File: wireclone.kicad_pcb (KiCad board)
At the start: 2 copper layers, 98.4 x 48.3 mm, 47 parts, among them P1 CONN_01X03, P2 CONN_01X02, P3 CONN_01X03, P4 CONN_01X02, U1 LME49720, U2 LME49720, U3 LME49600, U4 LME49600, U5 LM7812CT, U6 LM7912CT

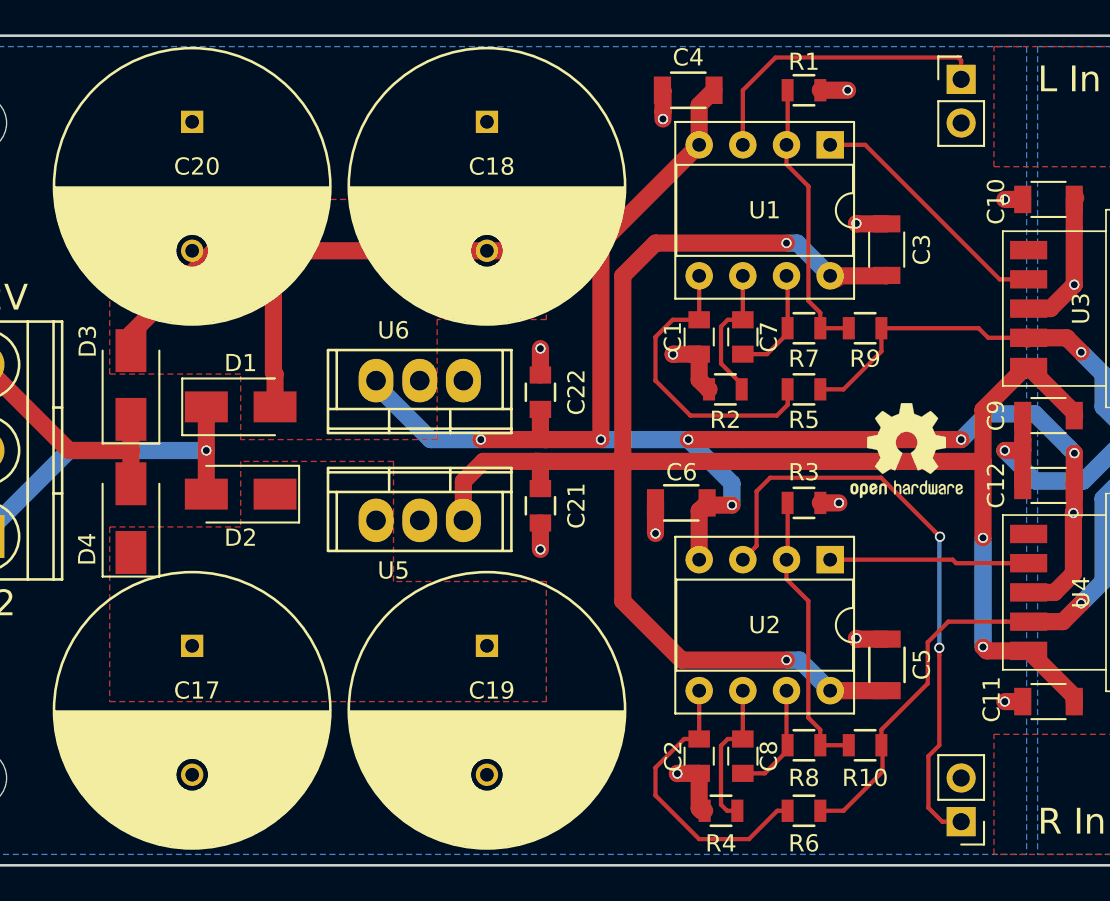
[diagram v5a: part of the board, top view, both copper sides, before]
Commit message: added fiducials
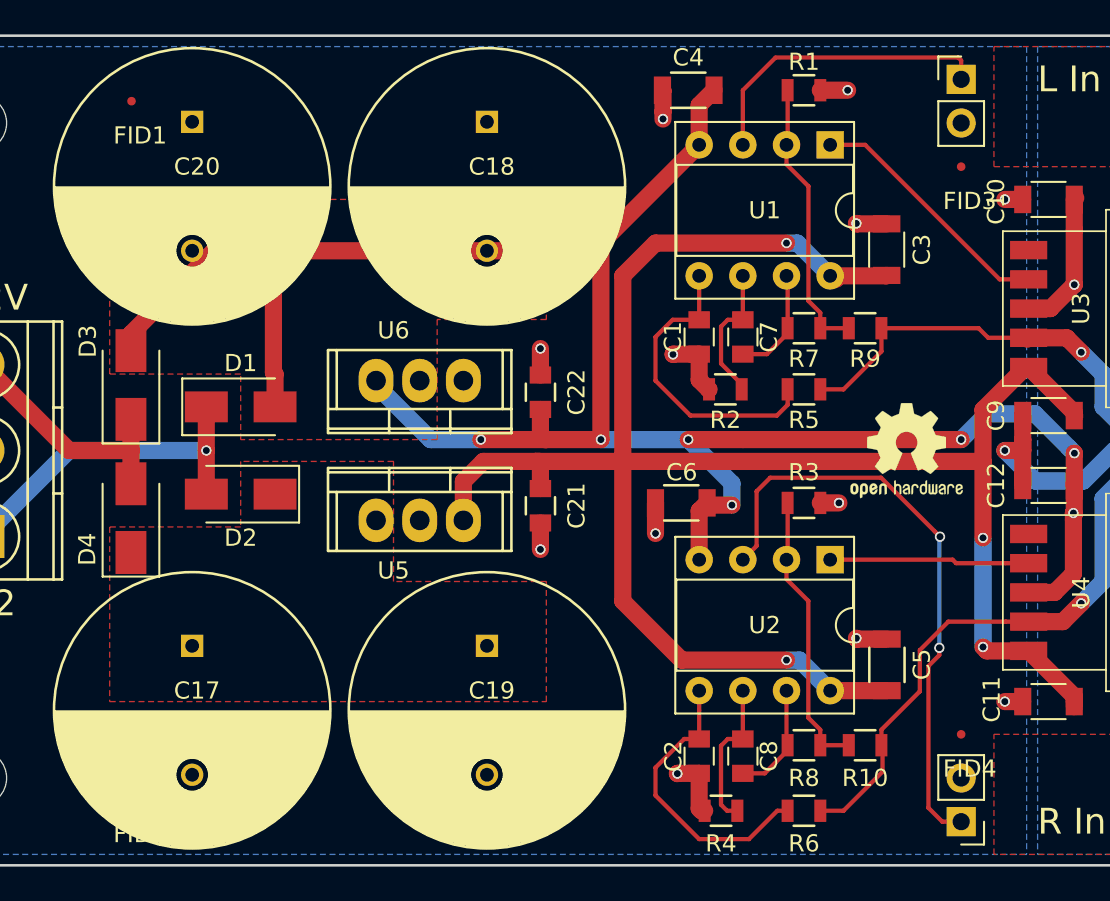
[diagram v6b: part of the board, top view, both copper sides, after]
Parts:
- added FID1: FIDUCIAL, smd:FID0.5, F.Cu at (71.1, 30.5)
- added FID2: FIDUCIAL, smd:FID0.5, F.Cu at (71.1, 71.1)
- added FID3: FIDUCIAL, smd:FID0.5, F.Cu at (119.4, 34.3)
- added FID4: FIDUCIAL, smd:FID0.5, F.Cu at (119.4, 67.3)
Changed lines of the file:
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@@
     (links 87)
     (no_connects 0)
-    (area 54.859 25.855 166.42381 75.005001)
+    (area 54.859 25.455 156.848334 75.005001)
     (thickness 1.6)
     (drawings 18)
-    (tracks 520)
+    (tracks 519)
     (zones 0)
-    (modules 47)
+    (modules 51)
     (nets 24)
   )
@@
       (xy -0.304547 -2.749533) (xy -0.2815 -2.753453) (xy -0.244491 -2.755865) (xy -0.189856 -2.757135)
       (xy -0.113933 -2.757629) (xy -0.013056 -2.757714) (xy 0 -2.757714) (xy 0.10391 -2.757652)) (layer F.SilkS) (width 0.01))
+  )
+  (module smd:FID0.5 (layer F.Cu)
+    (at 71.12 30.48)
+    (tags "fid, fiducial")
+    (fp_text reference FID1 (at 0.5 2) (layer F.SilkS)
+      (effects (font (size 1 1) (thickness 0.15)))
+    )
+    (fp_text value FIDUCIAL (at 4.5 -4) (layer F.Fab)
+      (effects (font (size 1 1) (thickness 0.15)))
+    )
+    (pad F smd circle (at 0 0) (size 0.5 0.5) (layers F.Cu F.Mask)
+      (solder_mask_margin 1) (clearance 1))
+  )
+  (module smd:FID0.5 (layer F.Cu)
+    (at 71.12 71.12)
+    (tags "fid, fiducial")
+    (fp_text reference FID2 (at 0.5 2) (layer F.SilkS)
+      (effects (font (size 1 1) (thickness 0.15)))
+    )
+    (fp_text value FIDUCIAL (at 4.5 -4) (layer F.Fab)
+      (effects (font (size 1 1) (thickness 0.15)))
+    )
+    (pad F smd circle (at 0 0) (size 0.5 0.5) (layers F.Cu F.Mask)
+      (solder_mask_margin 1) (clearance 1))
+  )
+  (module smd:FID0.5 (layer F.Cu)
+    (at 119.38 34.29)
+    (tags "fid, fiducial")
+    (fp_text reference FID3 (at 0.5 2) (layer F.SilkS)
+      (effects (font (size 1 1) (thickness 0.15)))
+    )
+    (fp_text value FIDUCIAL (at 4.5 -4) (layer F.Fab)
+      (effects (font (size 1 1) (thickness 0.15)))
+    )
+    (pad F smd circle (at 0 0) (size 0.5 0.5) (layers F.Cu F.Mask)
+      (solder_mask_margin 1) (clearance 1))
+  )
+  (module smd:FID0.5 (layer F.Cu)
+    (at 119.38 67.31)
+    (tags "fid, fiducial")
+    (fp_text reference FID4 (at 0.5 2) (layer F.SilkS)
+      (effects (font (size 1 1) (thickness 0.15)))
+    )
+    (fp_text value FIDUCIAL (at 4.5 -4) (layer F.Fab)
+      (effects (font (size 1 1) (thickness 0.15)))
+    )
+    (pad F smd circle (at 0 0) (size 0.5 0.5) (layers F.Cu F.Mask)
+      (solder_mask_margin 1) (clearance 1))
   )
   (gr_text "Headphone Amplifier" (at 147.32 50.8 90) (layer F.SilkS)
@@
   (segment (start 106.68 33.02) (end 106.68 29.845) (width 0.25) (layer F.Cu) (net 12))
   (segment (start 106.68 29.845) (end 108.570068 27.954932) (width 0.25) (layer F.Cu) (net 12))
+  (segment (start 118.108589 62.703627) (end 118.108589 62.279363) (width 0.25) (layer F.Cu) (net 13))
+  (segment (start 118.28 72.39) (end 117.475 71.585) (width 0.25) (layer F.Cu) (net 13))
+  (segment (start 119.38 72.39) (end 118.28 72.39) (width 0.25) (layer F.Cu) (net 13))
+  (segment (start 117.475 63.337216) (end 118.108589 62.703627) (width 0.25) (layer F.Cu) (net 13))
+  (segment (start 117.475 71.585) (end 117.475 63.337216) (width 0.25) (layer F.Cu) (net 13))
   (segment (start 117.848869 55.514565) (end 118.148868 55.814564) (width 0.25) (layer F.Cu) (net 13))
   (segment (start 107.479999 53.175001) (end 108.272442 52.382558) (width 0.25) (layer F.Cu) (net 13))
@@
   (segment (start 108.272442 52.382558) (end 114.716862 52.382558) (width 0.25) (layer F.Cu) (net 13))
   (segment (start 118.108589 62.279363) (end 118.108589 55.854843) (width 0.25) (layer B.Cu) (net 13))
-  (segment (start 118.28 72.39) (end 117.475 71.585) (width 0.25) (layer F.Cu) (net 13))
   (via (at 118.108589 62.279363) (size 0.6) (drill 0.4) (layers F.Cu B.Cu) (net 13))
-  (segment (start 118.108589 62.703627) (end 118.108589 62.279363) (width 0.25) (layer F.Cu) (net 13))
-  (segment (start 118.108589 67.946411) (end 118.108589 62.703627) (width 0.25) (layer F.Cu) (net 13))
-  (segment (start 117.475 68.58) (end 118.108589 67.946411) (width 0.25) (layer F.Cu) (net 13))
-  (segment (start 117.475 71.585) (end 117.475 68.58) (width 0.25) (layer F.Cu) (net 13))
-  (segment (start 119.38 72.39) (end 118.28 72.39) (width 0.25) (layer F.Cu) (net 13))
   (segment (start 128.905 49.53) (end 129.794 49.53) (width 1) (layer B.Cu) (net 14))
   (segment (start 150.47501 49.54999) (end 150.915001 49.109999) (width 1) (layer B.Cu) (net 14))
@@
   (segment (start 112.536 47.244) (end 114.742 45.038) (width 0.25) (layer F.Cu) (net 14))
   (segment (start 114.742 45.038) (end 114.742 43.688) (width 0.25) (layer F.Cu) (net 14))
+  (segment (start 121.975 60.755) (end 123.305 60.755) (width 0.25) (layer F.Cu) (net 15))
+  (segment (start 118.633948 60.755) (end 121.975 60.755) (width 0.25) (layer F.Cu) (net 15))
+  (segment (start 116.974989 62.413959) (end 118.633948 60.755) (width 0.25) (layer F.Cu) (net 15))
+  (segment (start 116.974989 64.812011) (end 116.974989 62.413959) (width 0.25) (layer F.Cu) (net 15))
+  (segment (start 114.742 67.045) (end 116.974989 64.812011) (width 0.25) (layer F.Cu) (net 15))
+  (segment (start 114.742 67.945) (end 114.742 67.045) (width 0.25) (layer F.Cu) (net 15))
   (segment (start 126.365 59.69) (end 127.635 58.42) (width 1) (layer B.Cu) (net 15))
   (segment (start 127.635 58.42) (end 127.635 53.590919) (width 1) (layer B.Cu) (net 15))
@@
   (segment (start 148.645 52.07) (end 149.915 53.34) (width 1) (layer B.Cu) (net 15))
   (segment (start 149.915 53.34) (end 151.765 53.34) (width 1) (layer B.Cu) (net 15))
-  (segment (start 121.975 60.755) (end 123.305 60.755) (width 0.25) (layer F.Cu) (net 15))
-  (segment (start 118.633948 60.755) (end 121.975 60.755) (width 0.25) (layer F.Cu) (net 15))
-  (segment (start 117.433587 61.955361) (end 118.633948 60.755) (width 0.25) (layer F.Cu) (net 15))
-  (segment (start 114.742 67.045) (end 117.433587 64.353413) (width 0.25) (layer F.Cu) (net 15))
-  (segment (start 117.433587 64.353413) (end 117.433587 61.955361) (width 0.25) (layer F.Cu) (net 15))
-  (segment (start 114.742 67.945) (end 114.742 67.045) (width 0.25) (layer F.Cu) (net 15))
   (segment (start 114.808 68.311) (end 114.808 69.483) (width 0.25) (layer F.Cu) (net 15))
   (segment (start 114.808 69.483) (end 112.536 71.755) (width 0.25) (layer F.Cu) (net 15))

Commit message: cleanup, rev.a as manufactured
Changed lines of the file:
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@@
     (at 71.12 30.48)
     (tags "fid, fiducial")
-    (fp_text reference FID1 (at 0.5 2) (layer F.SilkS)
+    (fp_text reference FID1 (at 0.5 2) (layer F.SilkS) hide
       (effects (font (size 1 1) (thickness 0.15)))
     )
@@
     (at 71.12 71.12)
     (tags "fid, fiducial")
-    (fp_text reference FID2 (at 0.5 2) (layer F.SilkS)
+    (fp_text reference FID2 (at 0.5 2) (layer F.SilkS) hide
       (effects (font (size 1 1) (thickness 0.15)))
     )
@@
     (at 119.38 34.29)
     (tags "fid, fiducial")
-    (fp_text reference FID3 (at 0.5 2) (layer F.SilkS)
+    (fp_text reference FID3 (at 0.5 2) (layer F.SilkS) hide
       (effects (font (size 1 1) (thickness 0.15)))
     )
@@
     (at 119.38 67.31)
     (tags "fid, fiducial")
-    (fp_text reference FID4 (at 0.5 2) (layer F.SilkS)
+    (fp_text reference FID4 (at 0.5 2) (layer F.SilkS) hide
       (effects (font (size 1 1) (thickness 0.15)))
     )

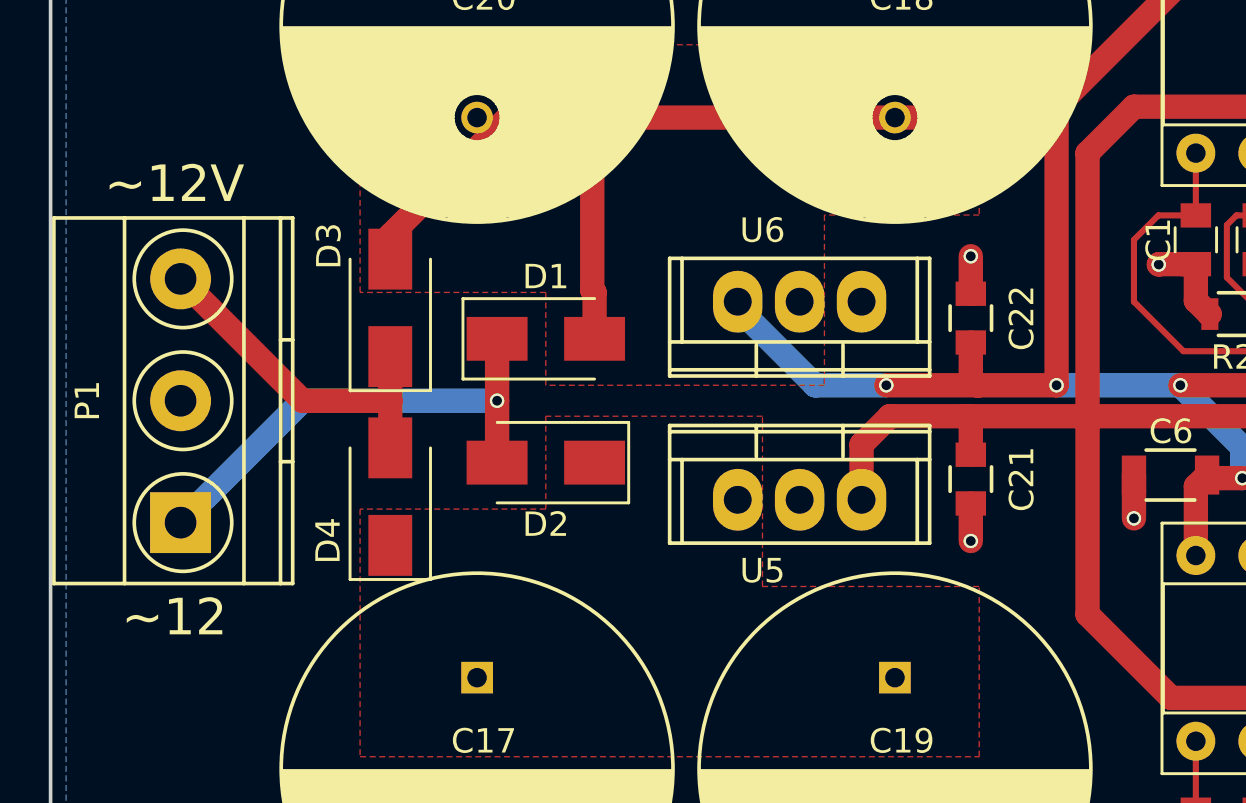
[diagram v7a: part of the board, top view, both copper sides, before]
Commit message: added reverse protection diodes to regulators, bumped to Rev.B
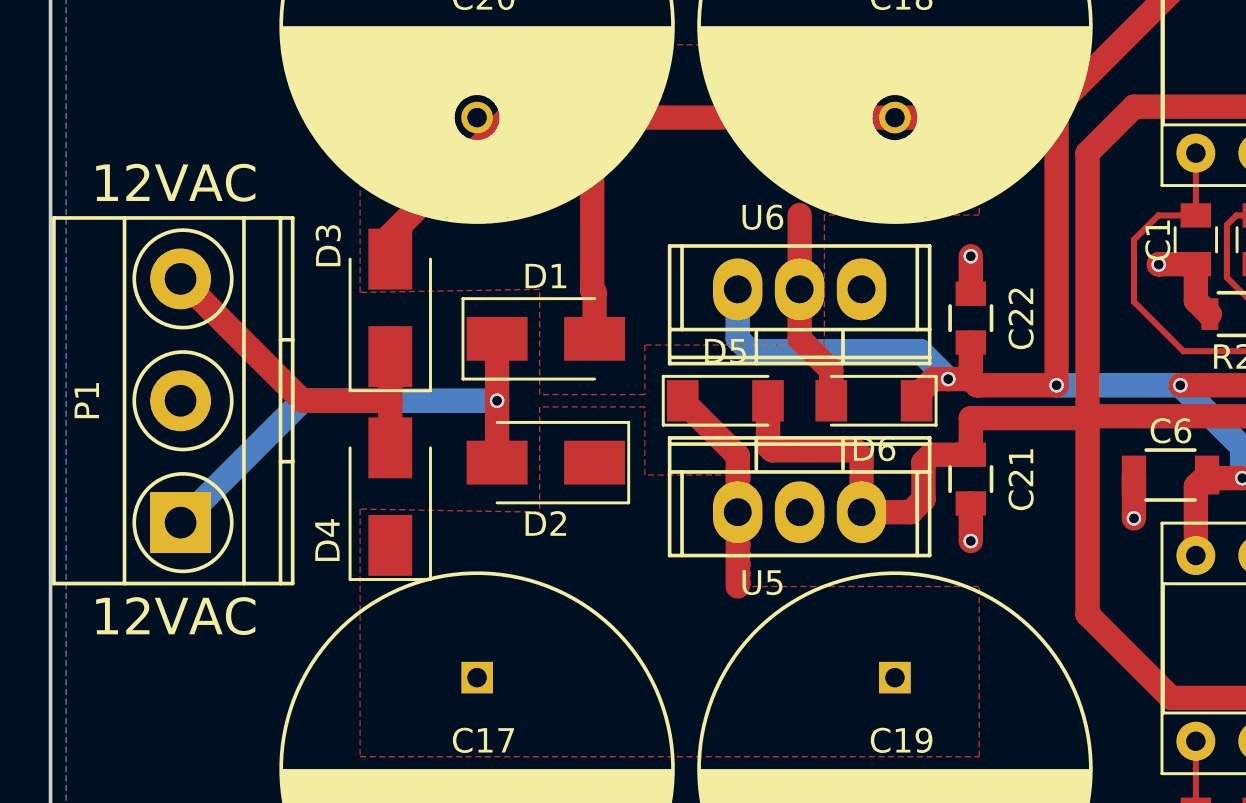
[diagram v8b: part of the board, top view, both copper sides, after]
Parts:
- added D5: LL4148, Diodes_SMD:D_MiniMELF, F.Cu at (84.8, 50.8)
- added D6: LL4148, Diodes_SMD:D_MiniMELF, F.Cu at (90.9, 50.8)
- moved U5 0.51 mm to (87.9, 55.4)
- moved U6 0.51 mm to (87.9, 46.2)
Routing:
- net Net-(C17-Pad1): track 0.00 -> 8.56 mm
- net Net-(C18-Pad2): track 34.1 -> 42.2 mm
- net /PSU/VCC: track 117.4 -> 124.4 mm
- net /PSU/VEE: track 459.3 -> 462.2 mm
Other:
- board text added: "12VAC"
- board text added: "Rev.B 201712"
- board text removed: "Rev.A 201710"
- board text removed: "~~12"
- board text removed: "~~12V"
